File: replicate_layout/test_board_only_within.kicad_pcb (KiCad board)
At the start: 2 copper layers, 30 parts, among them J1001 Pusa_4mm, J1002 Pusa_4mm, Q1001 CSD19531KCS, Q1002 CSD19531KCS, Q1003 CSD19531KCS, Q2001 CSD19531KCS, Q2002 CSD19531KCS, Q3001 CSD19531KCS, Q3002 CSD19531KCS, Q4001 CSD19531KCS, Q4002 CSD19531KCS, U1001 LAUNCHXL-F28377S, U2001 IR2181, U3001 IR2181, U4001 IR2181

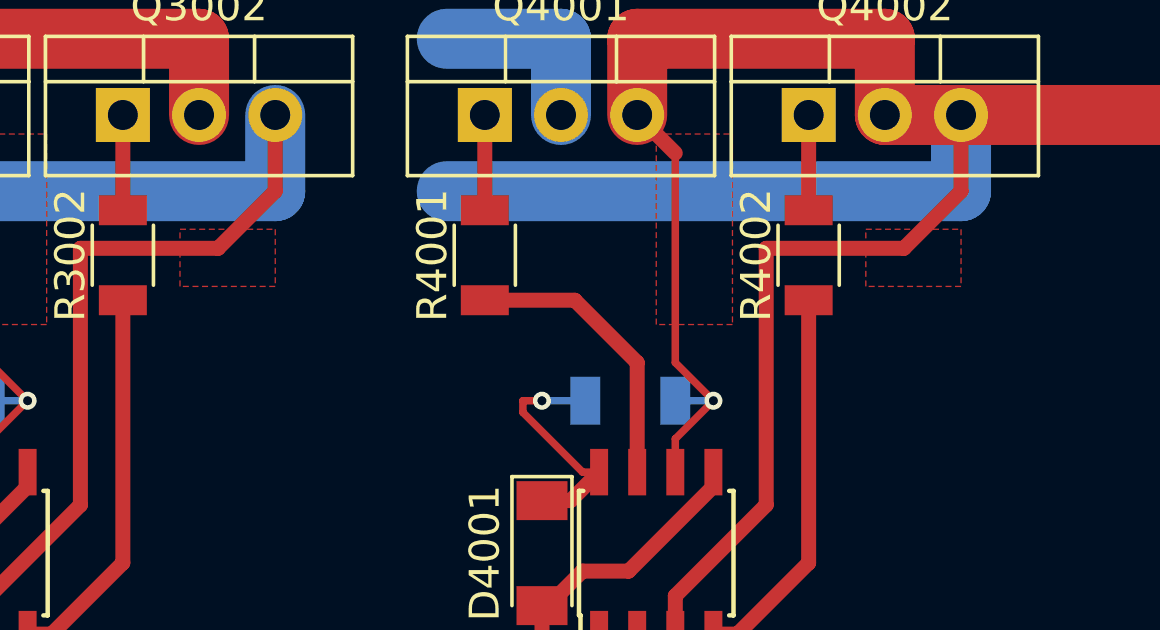
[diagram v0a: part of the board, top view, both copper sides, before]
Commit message: fixed a bug in test function changed how bounding box is calculated
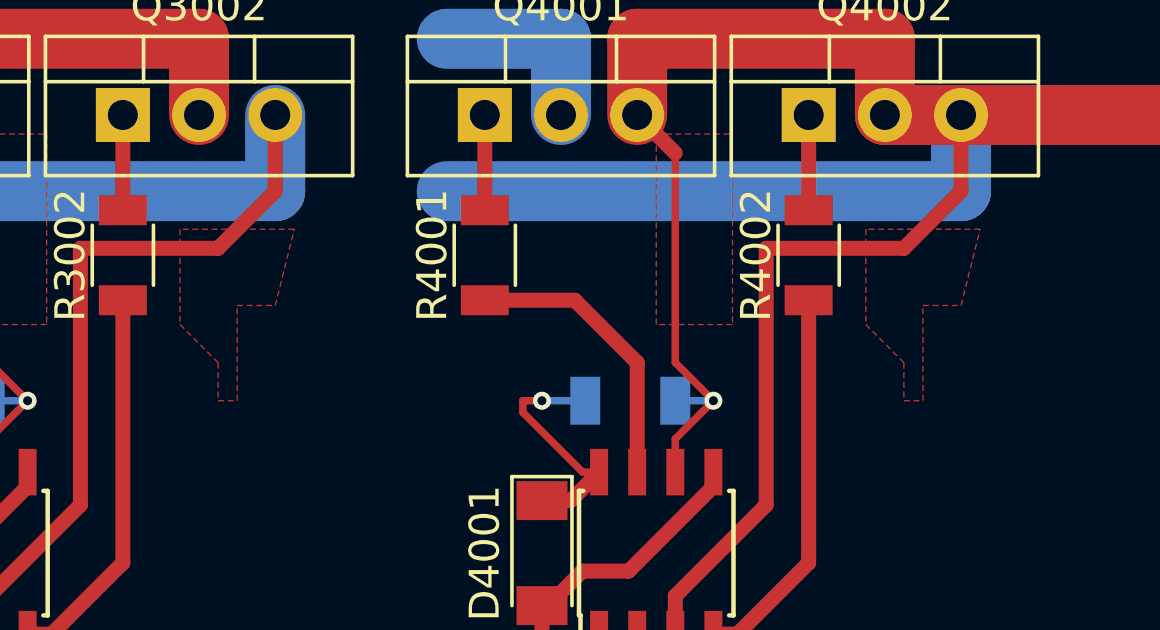
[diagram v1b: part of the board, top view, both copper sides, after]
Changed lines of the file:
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@@
     (polygon
       (pts
-        (xy 234.315 92.075) (xy 234.315 90.17) (xy 237.49 90.17) (xy 237.49 92.075)
+        (xy 234.315 90.17) (xy 234.315 93.345) (xy 235.585 94.615) (xy 235.585 95.885) (xy 236.22 95.885)
+        (xy 236.22 92.71) (xy 237.49 92.71) (xy 238.125 90.17)
       )
     )
@@
     (polygon
       (pts
-        (xy 211.455 92.075) (xy 211.455 90.17) (xy 214.63 90.17) (xy 214.63 92.075)
+        (xy 211.455 90.17) (xy 211.455 93.345) (xy 212.725 94.615) (xy 212.725 95.885) (xy 213.36 95.885)
+        (xy 213.36 92.71) (xy 214.63 92.71) (xy 215.265 90.17)
       )
     )

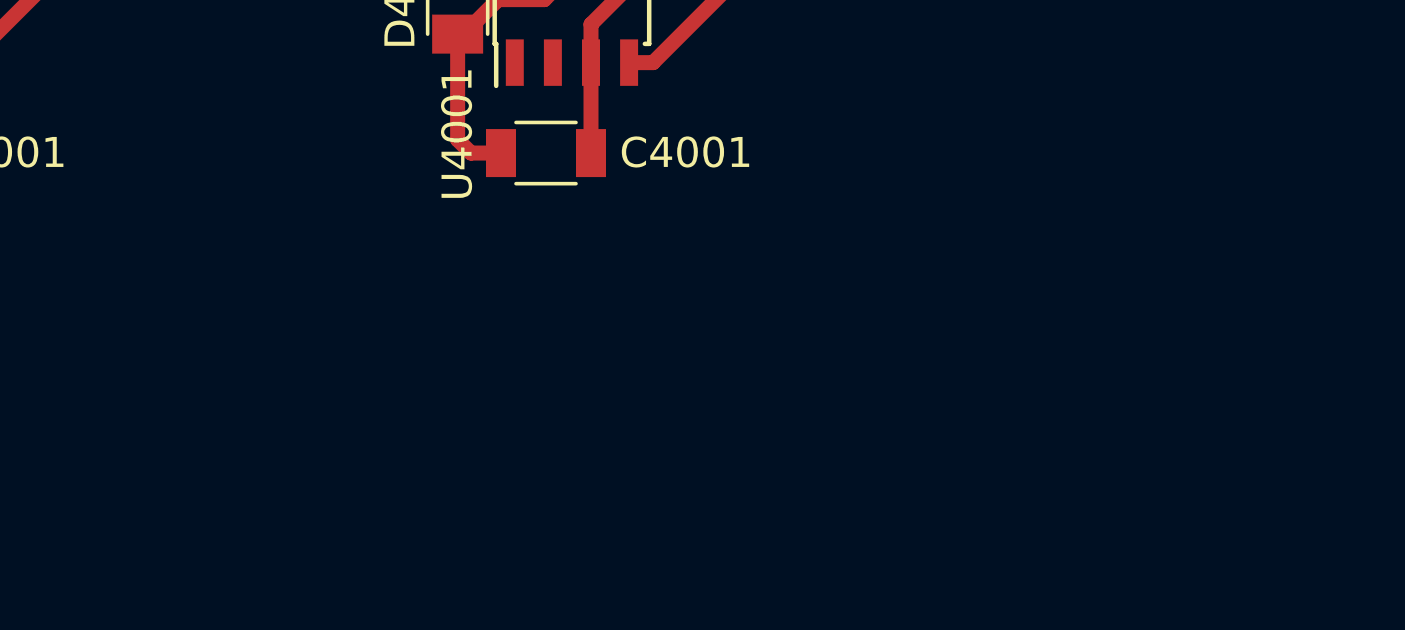
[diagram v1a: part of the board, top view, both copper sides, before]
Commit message: Pre-fill minimum replication steps. Modifed test cases
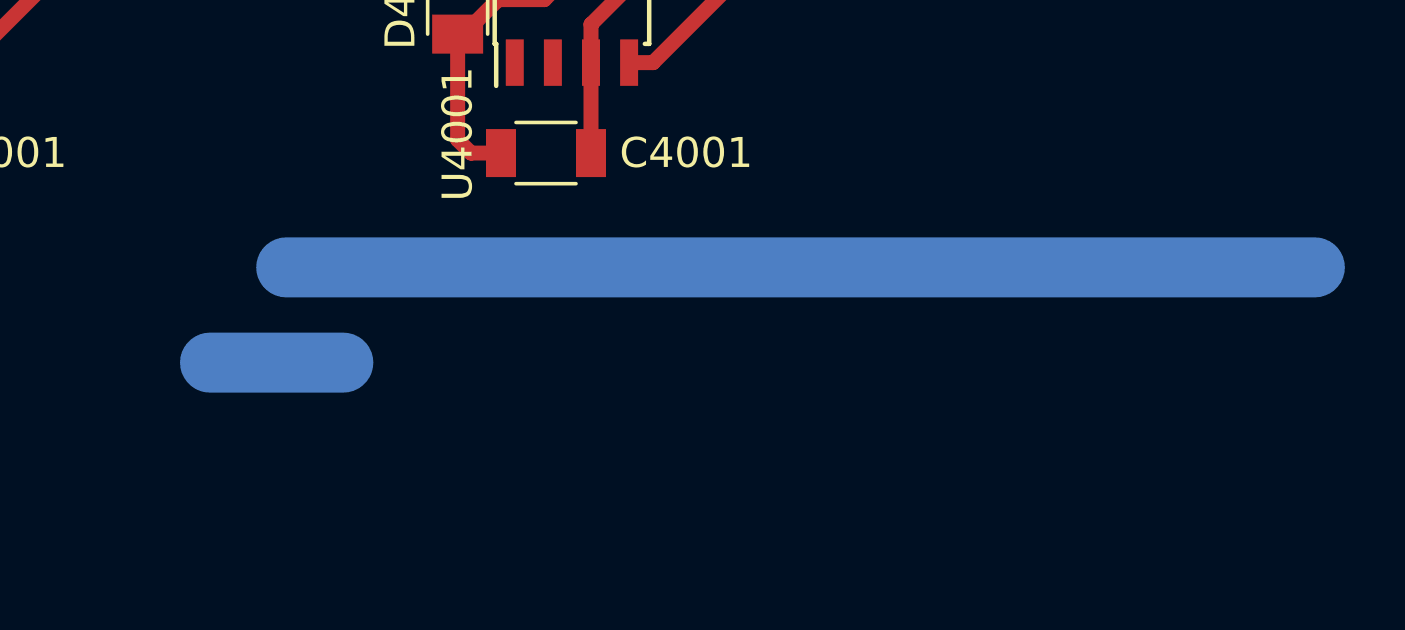
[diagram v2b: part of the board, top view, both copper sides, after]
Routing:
- net (no net): track 0.00 -> 38.7 mm

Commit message: Updated documentation
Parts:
- moved C4001 4.28 mm to (230.7, 106.7)
- moved C4002 4.28 mm to (230.7, 95.9)
- moved D4001 4.28 mm to (227.8, 101.0)
- moved Q4001 4.28 mm to (225.9, 86.4)
- moved Q4002 4.28 mm to (236.7, 86.4)
- moved R4001 4.28 mm to (225.9, 91.0)
- moved R4002 4.28 mm to (236.7, 91.0)
- moved U4001 4.28 mm to (231.6, 101.0)
- moved C3001 2.14 mm to (205.7, 106.7)
- moved C3002 2.14 mm to (205.7, 95.9)
- moved D3001 2.14 mm to (202.8, 101.0)
- moved Q3001 2.14 mm to (200.9, 86.4)
- moved R3001 2.14 mm to (200.9, 91.0)
- moved U3001 2.14 mm to (206.6, 101.0)
- moved Q3002 2.14 mm to (211.7, 86.4)
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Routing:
- net /Veja_3/OUT: track 40.2 -> 28.1 mm
- net (no net): track 38.7 -> 50.8 mm

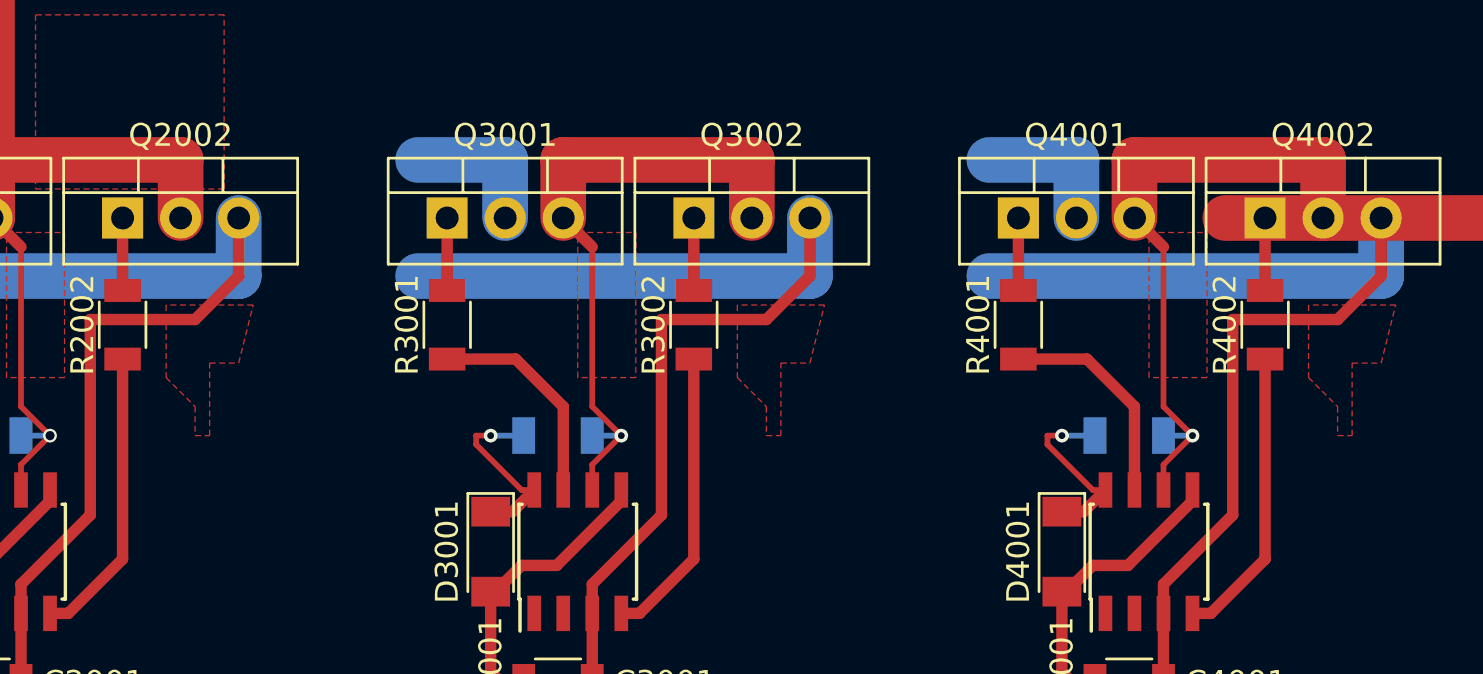
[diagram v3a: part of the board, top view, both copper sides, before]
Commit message: Bugfix for circular module orientation in linear replication
Updated test layouts as it tests for non copper zones also
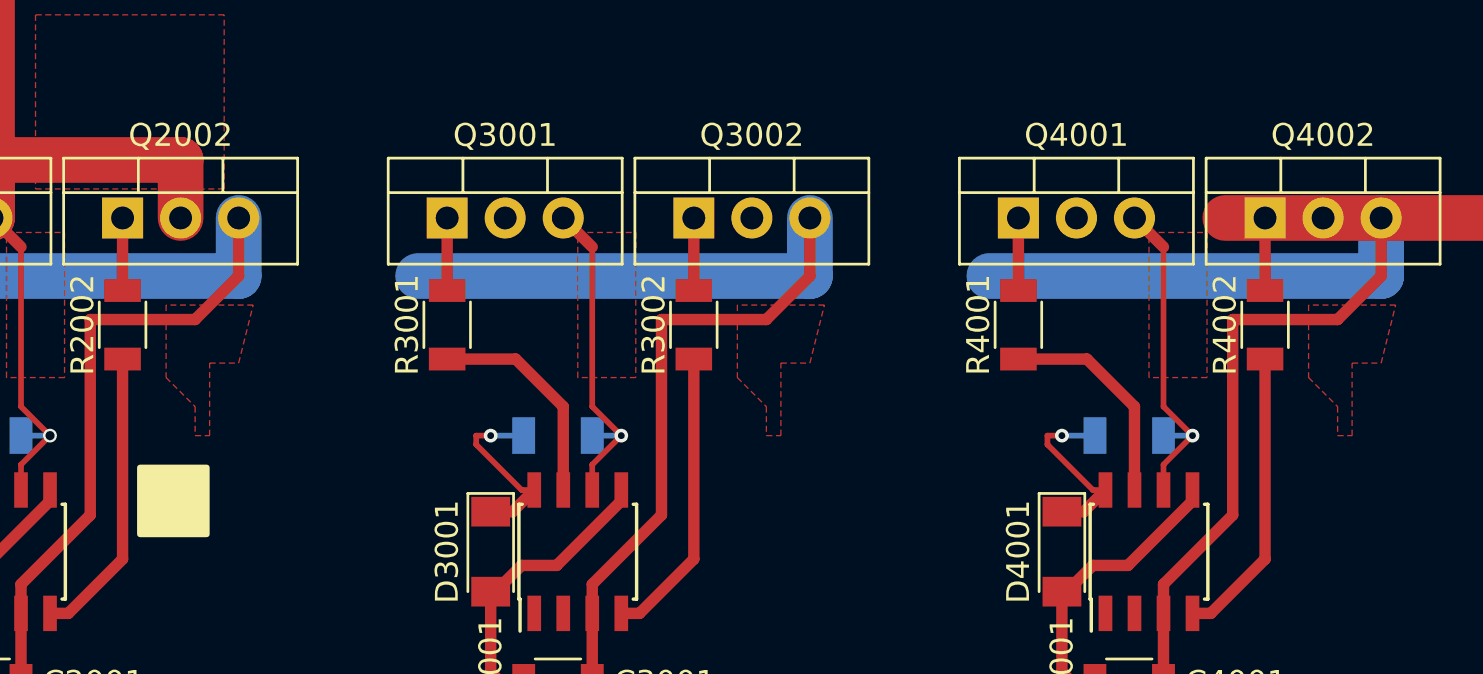
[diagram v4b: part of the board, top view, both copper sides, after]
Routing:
- net (no net): track 50.8 -> 0.00 mm
- net +VDC: track 27.2 -> 65.3 mm
- net /Veja_3/OUT: track 28.1 -> 14.8 mm
- net /Veja_2/OUT: track 28.1 -> 14.8 mm
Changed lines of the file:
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@@
     (thickness 1.6)
     (drawings 0)
-    (tracks 143)
+    (tracks 133)
     (zones 0)
     (modules 30)
@@
   (segment (start 227.165 95.885) (end 227.8 95.885) (width 0.25) (layer F.Cu) (net 12))
   (segment (start 227.8 95.885) (end 229.245 95.885) (width 0.25) (layer B.Cu) (net 12))
-  (segment (start 228.435 83.82) (end 228.435 86.36) (width 2) (layer B.Cu) (net 5))
-  (segment (start 224.625 83.82) (end 228.435 83.82) (width 2) (layer B.Cu) (net 5))
   (segment (start 230.975 86.36) (end 232.245 87.63) (width 0.5) (layer F.Cu) (net 13))
   (via (at 233.515 95.885) (size 0.6) (layers F.Cu B.Cu) (net 13))
@@
   (segment (start 232.245 94.615) (end 233.515 95.885) (width 0.25) (layer F.Cu) (net 13))
   (segment (start 232.245 87.63) (end 232.245 94.615) (width 0.25) (layer F.Cu) (net 13))
-  (segment (start 239.23 83.82) (end 239.23 86.36) (width 2) (layer F.Cu) (net 13))
-  (segment (start 230.975 83.82) (end 239.23 83.82) (width 2) (layer F.Cu) (net 13))
-  (segment (start 230.975 86.36) (end 230.975 83.82) (width 2) (layer F.Cu) (net 13))
   (segment (start 232.245 106.68) (end 232.245 103.665) (width 0.5) (layer F.Cu) (net 2))
   (segment (start 241.77 88.9) (end 241.77 86.36) (width 2) (layer B.Cu) (net 2))
@@
   (segment (start 202.165 95.885) (end 202.8 95.885) (width 0.25) (layer F.Cu) (net 11))
   (segment (start 202.8 95.885) (end 204.245 95.885) (width 0.25) (layer B.Cu) (net 11))
-  (segment (start 203.435 83.82) (end 203.435 86.36) (width 2) (layer B.Cu) (net 5))
-  (segment (start 199.625 83.82) (end 203.435 83.82) (width 2) (layer B.Cu) (net 5))
   (segment (start 205.975 86.36) (end 207.245 87.63) (width 0.5) (layer F.Cu) (net 4))
   (via (at 208.515 95.885) (size 0.6) (layers F.Cu B.Cu) (net 4))
@@
   (segment (start 207.245 94.615) (end 208.515 95.885) (width 0.25) (layer F.Cu) (net 4))
   (segment (start 207.245 87.63) (end 207.245 94.615) (width 0.25) (layer F.Cu) (net 4))
-  (segment (start 214.23 83.82) (end 214.23 86.36) (width 2) (layer F.Cu) (net 4))
-  (segment (start 205.975 83.82) (end 214.23 83.82) (width 2) (layer F.Cu) (net 4))
-  (segment (start 205.975 86.36) (end 205.975 83.82) (width 2) (layer F.Cu) (net 4))
   (segment (start 207.245 106.68) (end 207.245 103.665) (width 0.5) (layer F.Cu) (net 2))
   (segment (start 216.77 88.9) (end 216.77 86.36) (width 2) (layer B.Cu) (net 2))
@@
   (segment (start 202.8 106.235) (end 203.245 106.68) (width 0.5) (layer F.Cu) (net 1))
   (segment (start 202.8 102.715) (end 202.8 106.235) (width 0.5) (layer F.Cu) (net 1))
-  (segment (start 215.265 113.665) (end 219.71 113.665) (width 2) (layer B.Cu) (net 0))
-  (segment (start 217.805 110.49) (end 252.095 110.49) (width 2) (layer B.Cu) (net 0))
-  (segment (start 247.015 86.36) (end 234.95 86.36) (width 2) (layer F.Cu) (net 0))
+  (segment (start 215.265 113.665) (end 219.71 113.665) (width 2) (layer B.Cu) (net 5))
+  (segment (start 217.805 110.49) (end 252.095 110.49) (width 2) (layer B.Cu) (net 5))
+  (segment (start 247.015 86.36) (end 234.95 86.36) (width 2) (layer F.Cu) (net 5))
   (segment (start 177.8 102.715) (end 177.8 106.235) (width 0.5) (layer F.Cu) (net 1))
   (segment (start 177.8 106.235) (end 178.245 106.68) (width 0.5) (layer F.Cu) (net 1))
@@
     )
   )
+  (zone (net 0) (net_name "") (layer F.SilkS) (hatch edge 0.508)
+    (connect_pads (clearance 0.508))
+    (min_thickness 0.254)
+    (fill (arc_segments 16) (thermal_gap 0.508) (thermal_bridge_width 0.508))
+    (polygon
+      (pts
+        (xy 237.325 97.155) (xy 240.5 97.155) (xy 240.5 100.33) (xy 237.325 100.33)
+      )
+    )
+  )
   (zone (net 13) (net_name /Veja_3/OUT) (layer F.Cu) (hatch edge 0.508)
     (connect_pads (clearance 0.508))
@@
     )
   )
+  (zone (net 0) (net_name "") (layer F.SilkS) (hatch edge 0.508)
+    (connect_pads (clearance 0.508))
+    (min_thickness 0.254)
+    (fill (arc_segments 16) (thermal_gap 0.508) (thermal_bridge_width 0.508))
+    (polygon
+      (pts
+        (xy 212.325 97.155) (xy 215.5 97.155) (xy 215.5 100.33) (xy 212.325 100.33)
+      )
+    )
+  )
   (zone (net 4) (net_name /Veja_2/OUT) (layer F.Cu) (hatch edge 0.508)
     (connect_pads (clearance 0.508))
@@
       )
     )
+  )
+  (zone (net 0) (net_name "") (layer F.SilkS) (hatch edge 0.508)
+    (connect_pads (clearance 0.508))
+    (min_thickness 0.254)
+    (fill yes (arc_segments 16) (thermal_gap 0.508) (thermal_bridge_width 0.508))
+    (polygon
+      (pts
+        (xy 187.325 97.155) (xy 190.5 97.155) (xy 190.5 100.33) (xy 187.325 100.33)
+      )
+    )
